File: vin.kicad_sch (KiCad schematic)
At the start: 35 parts, among them J4 USB4105, J5 Barrel_Jack_Switch, Q1 SiSA35DN, U14 D5V0H1B2LP, U15 TPS54233, U16 TPS2116DRLR, U17 INA219BxD

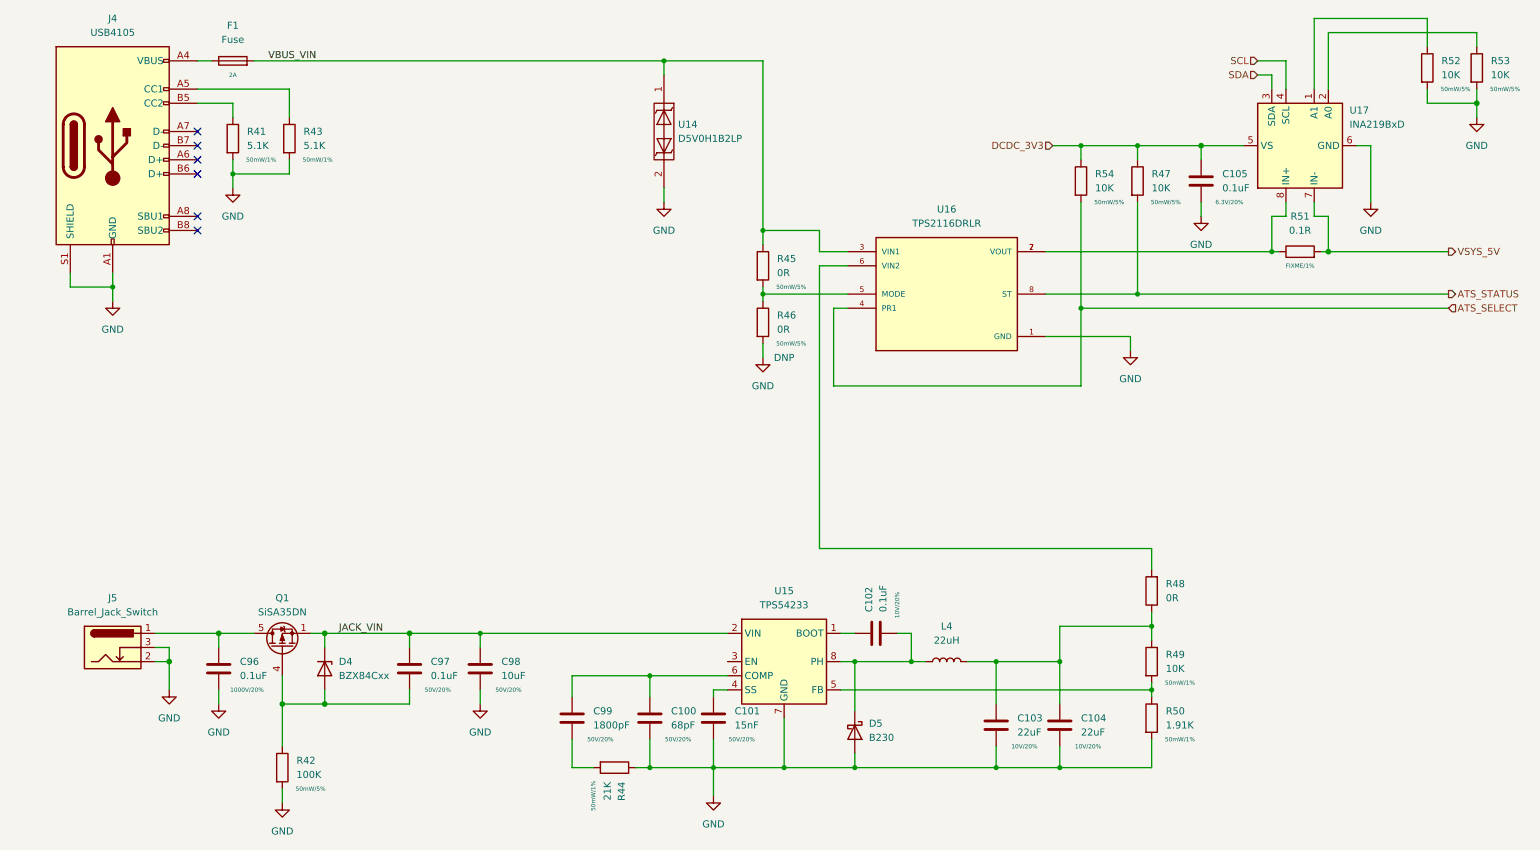
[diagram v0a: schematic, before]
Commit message: start moving to hierarchal labels, add emmc
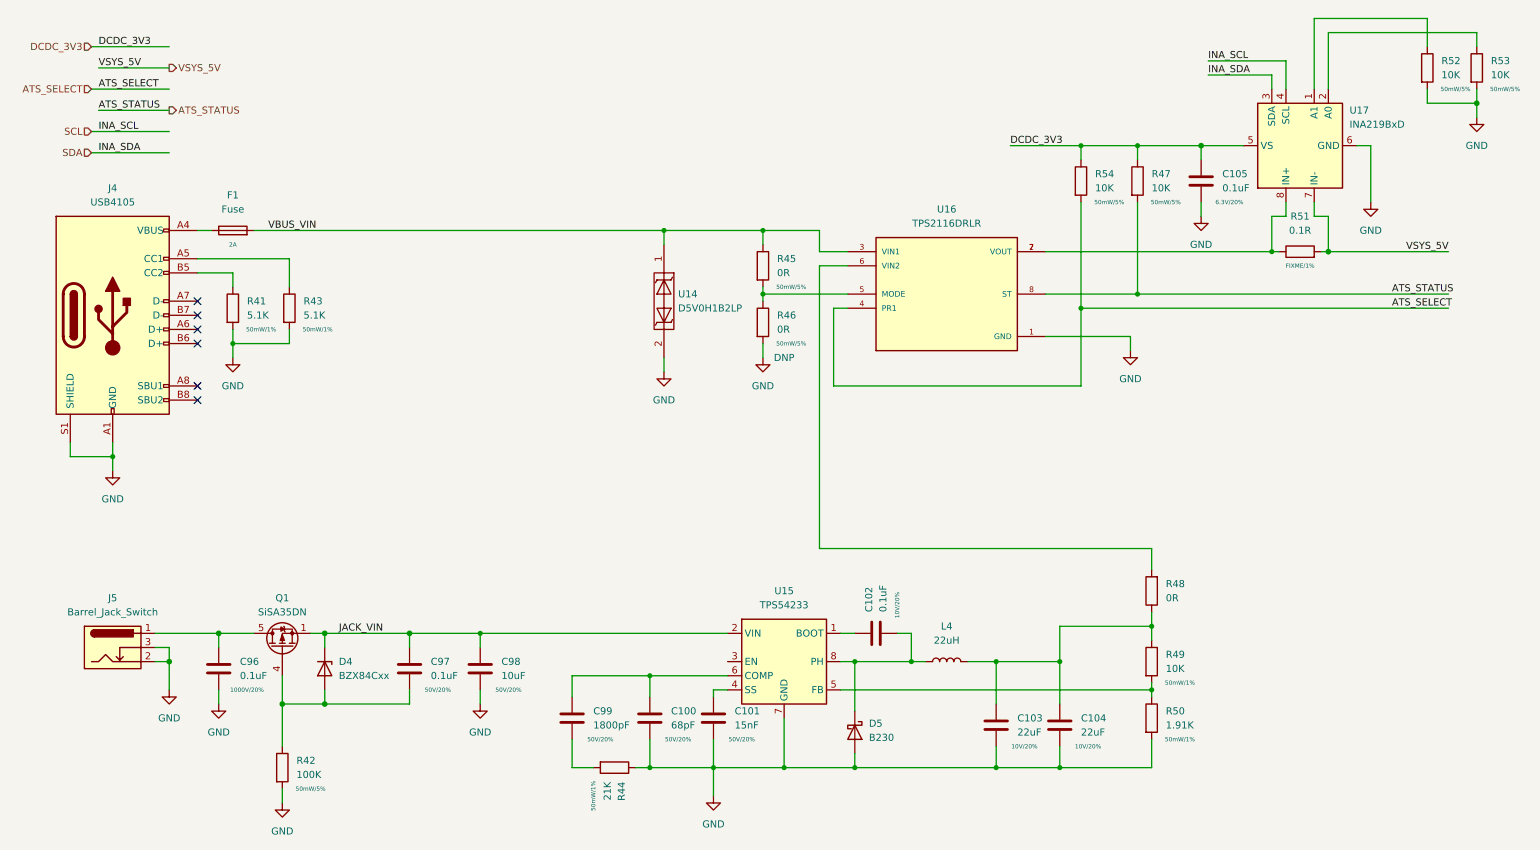
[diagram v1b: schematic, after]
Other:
- moved on the sheet: F1, J4, R41, R43, U14

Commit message: move to hierarchal labels, work on power tree, add basic pcb layout
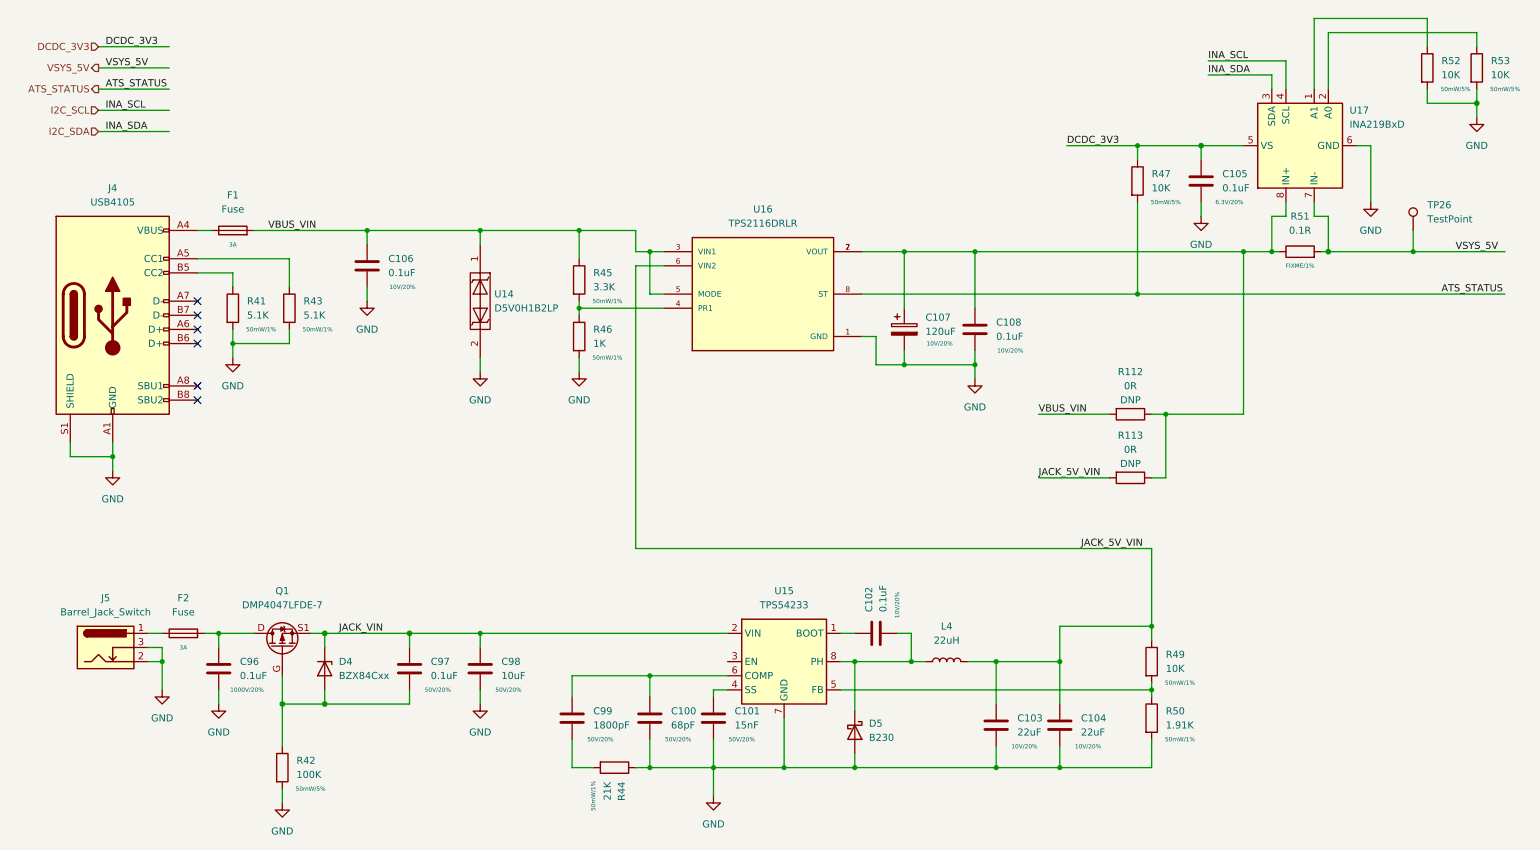
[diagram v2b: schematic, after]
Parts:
- removed Q1: SiSA35DN, Package_SO:Vishay_PowerPAK_1212-8_Single, symbol dNAS-CM4:SiSA35DN
- removed R48: 0R, Resistor_SMD:R_0805_2012Metric, symbol Device:R
- removed R54: 10K, Resistor_SMD:R_0402_1005Metric, symbol Device:R
- added C106, C108: 0.1uF, Capacitor_SMD:C_0402_1005Metric, symbol Device:C
- added C107: 120uF, Capacitor_SMD:CP_Elec_5x5.8, symbol Device:C_Polarized
- added F2: Fuse, Fuse:Fuse_0805_2012Metric, symbol Device:Fuse
- added Q1: DMP4047LFDE-7, imx6ull-sbc:6-PowerUDFN, symbol imx6ull-sbc:DMP4047LFDE-7
- added R112, R113: 0R, Resistor_SMD:R_0603_1608Metric, symbol Device:R
- added TP26: TestPoint, TestPoint:TestPoint_Pad_D1.0mm, symbol Connector:TestPoint
- F1: Rating 2A -> 3A
- R45: value 0R -> 3.3K; Rating 50mW/5% -> 50mW/1%
- R46: value 0R -> 1K; DNP DNP -> (none); Rating 50mW/5% -> 50mW/1%
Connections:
- net ATS_SELECT is gone; now on an unnamed net: U16.4 (PR1)
- net GND: now also C106.2, C107.2, C108.2
- net JACK_VIN: now also Q1.S1 (S), Q1.S2 (S)
- net VBUS_VIN: now also U16.5 (MODE), C106.1, R112.2
- net VSYS_5V: now also TP26.1
- net at R45.2, R46.1: no longer U16.5 (MODE)
- net at J5.1: now also F2.1; no longer C96.1
- net JACK_5V_VIN: now reaches C103.1, C104.1, L4.2, R49.1
- net JACK_5V_VIN: now also U16.6 (VIN2), R113.2
- net at C97.2, D4.2 (A), R42.1: now also Q1.G
- net at R51.1, U16.2 (VOUT), U16.7 (VOUT)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: now also C107.1, C108.1, R112.1, R113.1
- net SCL renamed I2C_SCL
- net SDA renamed I2C_SDA
- new net: C96.1, F2.2, Q1.D
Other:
- moved on the sheet: J5, R45, R46, U14, U16

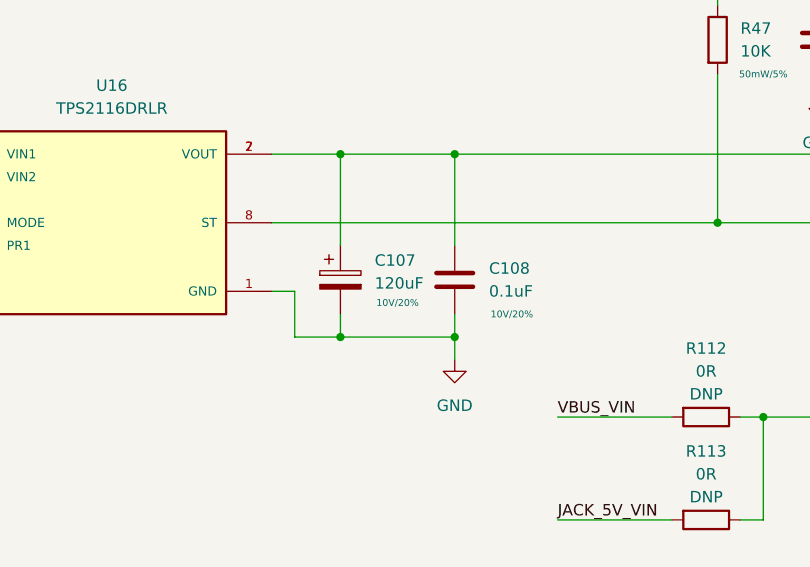
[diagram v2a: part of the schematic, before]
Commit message: most of sch done, inital component pcb placement
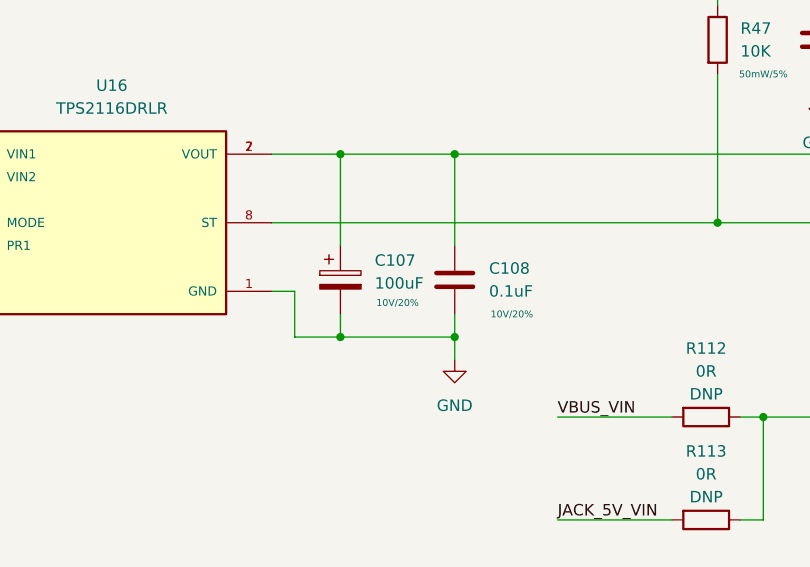
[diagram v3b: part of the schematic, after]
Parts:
- C107: value 120uF -> 100uF; footprint Capacitor_SMD:CP_Elec_5x5.8 -> Capacitor_Tantalum_SMD:CP_EIA-3528-15_AVX-H
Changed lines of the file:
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@@
-    (pin "2")
-  )
-  (symbol (lib_id "Device:C_Polarized") (at 172.72 73.66 0) (unit 1)
-    (in_bom yes) (on_board yes)
-    (property "Reference" "C107" (id 0) (at 176.53 71.5009 0)
-      (effects (font (size 1.27 1.27)) (justify left))
-    )
-    (property "Value" "120uF" (id 1) (at 176.53 74.0409 0)
-      (effects (font (size 1.27 1.27)) (justify left))
-    )
-    (property "Footprint" "Capacitor_SMD:CP_Elec_5x5.8" (id 2) (at 173.6852 77.47 0)
-      (effects (font (size 1.27 1.27)) hide)
-    )
-    (property "Datasheet" "~" (id 3) (at 172.72 73.66 0)
-      (effects (font (size 1.27 1.27)) hide)
-    )
-    (property "Rating" "10V/20%" (id 4) (at 179.07 76.2 0)
-      (effects (font (size 0.762 0.762)))
-    )
-    (pin "1")
     (pin "2")
   )
@@
     )
     (pin "1")
+    (pin "2")
+  )
+  (symbol (lib_id "Device:C_Polarized") (at 172.72 73.66 0) (unit 1)
+    (in_bom yes) (on_board yes)
+    (property "Reference" "C107" (id 0) (at 176.53 71.5009 0)
+      (effects (font (size 1.27 1.27)) (justify left))
+    )
+    (property "Value" "100uF" (id 1) (at 176.53 74.0409 0)
+      (effects (font (size 1.27 1.27)) (justify left))
+    )
+    (property "Footprint" "Capacitor_Tantalum_SMD:CP_EIA-3528-15_AVX-H" (id 2) (at 173.6852 77.47 0)
+      (effects (font (size 1.27 1.27)) hide)
+    )
+    (property "Datasheet" "~" (id 3) (at 172.72 73.66 0)
+      (effects (font (size 1.27 1.27)) hide)
+    )
+    (property "Rating" "10V/20%" (id 4) (at 179.07 76.2 0)
+      (effects (font (size 0.762 0.762)))
+    )
+    (pin "1")

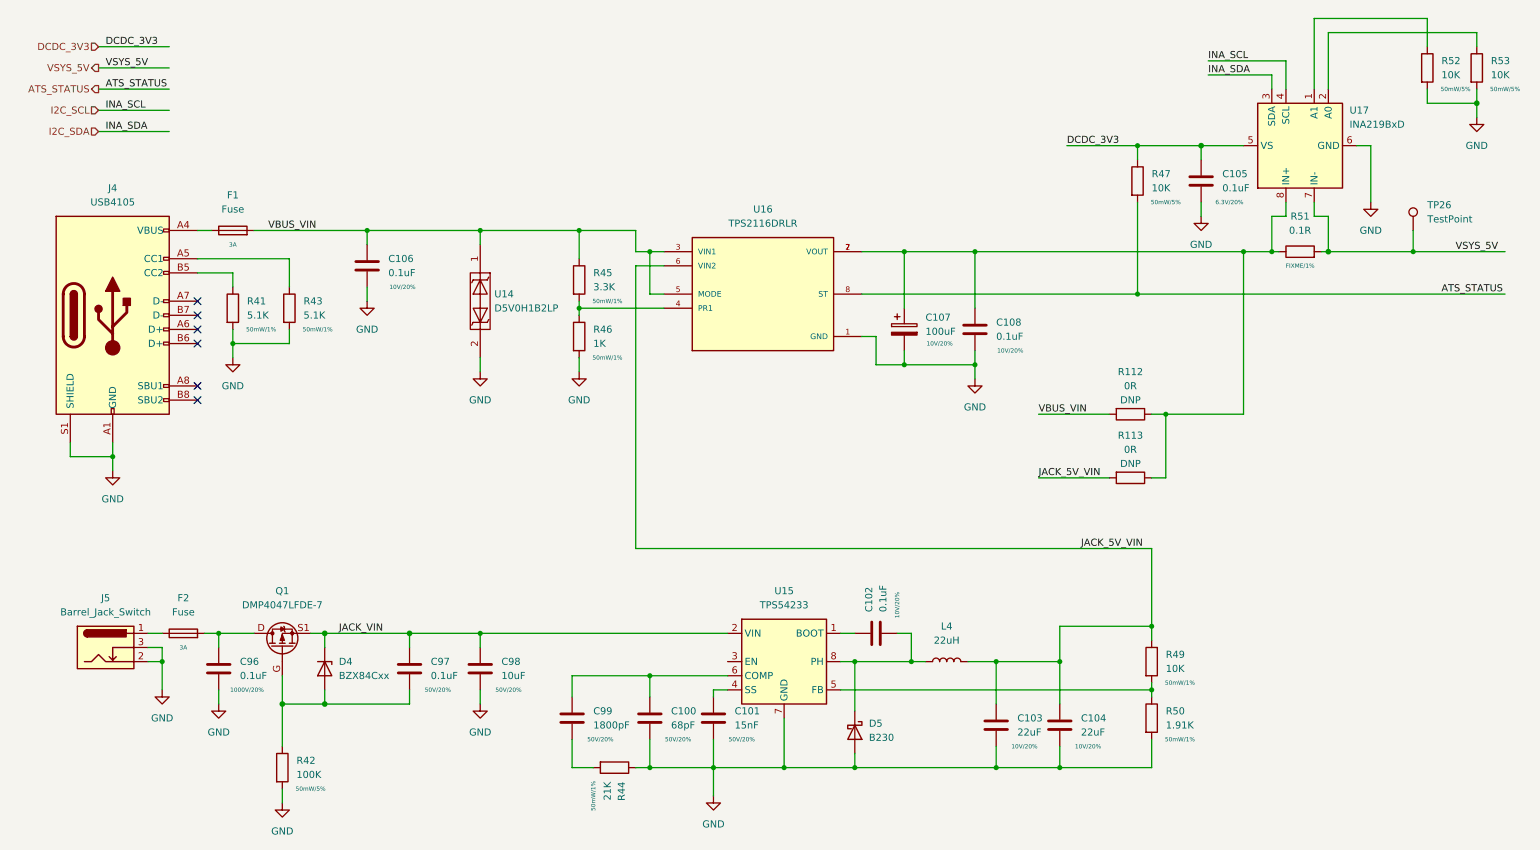
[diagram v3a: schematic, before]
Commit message: lots of routing, ddr length matching done
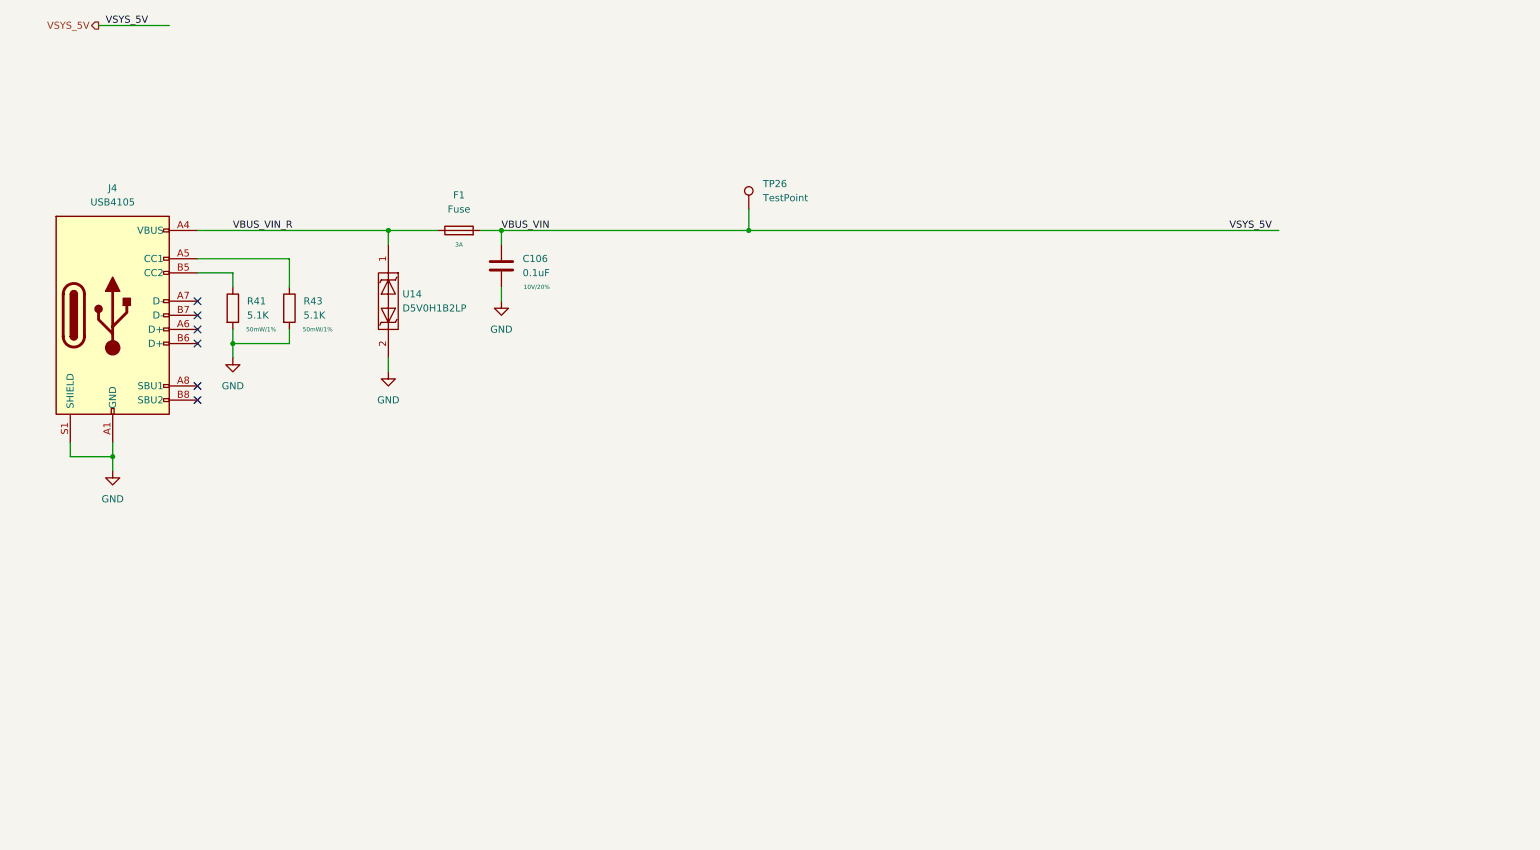
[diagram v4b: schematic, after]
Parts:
- removed C100: 68pF, Capacitor_SMD:C_0402_1005Metric, symbol Device:C
- removed C101: 15nF, Capacitor_SMD:C_0402_1005Metric, symbol Device:C
- removed C102, C105, C108: 0.1uF, Capacitor_SMD:C_0402_1005Metric, symbol Device:C
- removed C103, C104: 22uF, Capacitor_SMD:C_0805_2012Metric, symbol Device:C
- removed C107: 100uF, Capacitor_Tantalum_SMD:CP_EIA-3528-15_AVX-H, symbol Device:C_Polarized
- removed C96, C97: 0.1uF, Capacitor_SMD:C_0603_1608Metric, symbol Device:C
- removed C98: 10uF, Capacitor_SMD:C_1206_3216Metric, symbol Device:C
- removed C99: 1800pF, Capacitor_SMD:C_0402_1005Metric, symbol Device:C
- removed D4: BZX84Cxx, Diode_SMD:D_SOT-23_ANK, symbol Diode:BZX84Cxx
- removed D5: B230, Diode_SMD:D_SMB, symbol Diode:B230
- removed F2: Fuse, Fuse:Fuse_0805_2012Metric, symbol Device:Fuse
- removed J5: Barrel_Jack_Switch, imx6ull-sbc:TENSILITY_54-00167, symbol Connector:Barrel_Jack_Switch
- removed L4: 22uH, Inductor_SMD:L_Vishay_IHLP-2525, symbol Device:L
- removed Q1: DMP4047LFDE-7, imx6ull-sbc:6-PowerUDFN, symbol imx6ull-sbc:DMP4047LFDE-7
- removed R112, R113: 0R, Resistor_SMD:R_0603_1608Metric, symbol Device:R
- removed R42: 100K, Resistor_SMD:R_0402_1005Metric, symbol Device:R
- removed R44: 21K, Resistor_SMD:R_0402_1005Metric, symbol Device:R
- removed R45: 3.3K, Resistor_SMD:R_0402_1005Metric, symbol Device:R
- removed R46: 1K, Resistor_SMD:R_0402_1005Metric, symbol Device:R
- removed R47, R49, R52, R53: 10K, Resistor_SMD:R_0402_1005Metric, symbol Device:R
- removed R50: 1.91K, Resistor_SMD:R_0402_1005Metric, symbol Device:R
- removed R51: 0.1R, Resistor_SMD:R_1206_3216Metric, symbol Device:R
- removed U15: TPS54233, Package_SO:SOIC-8_3.9x4.9mm_P1.27mm, symbol Regulator_Switching:TPS54233
- removed U16: TPS2116DRLR, imx6ull-sbc:SOTFL50P160X60-8N, symbol imx6ull-sbc:TPS2116DRLR
- removed U17: INA219BxD, Package_SO:SOIC-8_3.9x4.9mm_P1.27mm, symbol Analog_ADC:INA219BxD
- U14: footprint imx6ull-sbc:DFN100X60X45-2N -> qsbc-zero:DFN100X60X45-2N; symbol imx6ull-sbc:D5V0H1B2LP -> qsbc-zero:D5V0H1B2LP
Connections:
- net VSYS_5V: now also C106.1, F1.2
- net VBUS_VIN_R: now reaches F1.1, J4.A4 (VBUS), J4.A9 (VBUS), J4.B4 (VBUS), J4.B9 (VBUS)
- net VBUS_VIN_R: now also U14.1
- removed net VBUS_VIN: C106.1, F1.2, U14.1
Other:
- moved on the sheet: C106, F1, TP26, U14
